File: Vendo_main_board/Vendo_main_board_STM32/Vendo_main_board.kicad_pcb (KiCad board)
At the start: 2 copper layers, 81.1 x 100 mm, 129 parts, among them J1 Screw_Terminal_01x04, J10 Screw_Terminal_01x03, J11 Screw_Terminal_01x02, J12 Screw_Terminal_01x03, J2 Barrel_Jack_MountingPin, J3 Conn_01x05_Pin, J4 Conn_01x05_Pin, J5 BOOT, J6 Screw_Terminal_01x04, J7 FTDI, J9 Conn_01x04_Pin, Q1 Q_NMOS_Depletion_GSD, Q2 Q_NMOS_Depletion_GSD, Q3 Q_NMOS_Depletion_GSD, Q4 Q_NMOS_Depletion_GSD, SW1 SW_Push, SW2 SW_Push, SW3 SW_Push, SW4 SW_Push, SW5 SW_Slide_DPDT, U1 AMS1117-3.3, U2 TPS54331D, U3 STM32F103C8T6, U4 PC817, Y1 32.768kHz, Y2 8MHz

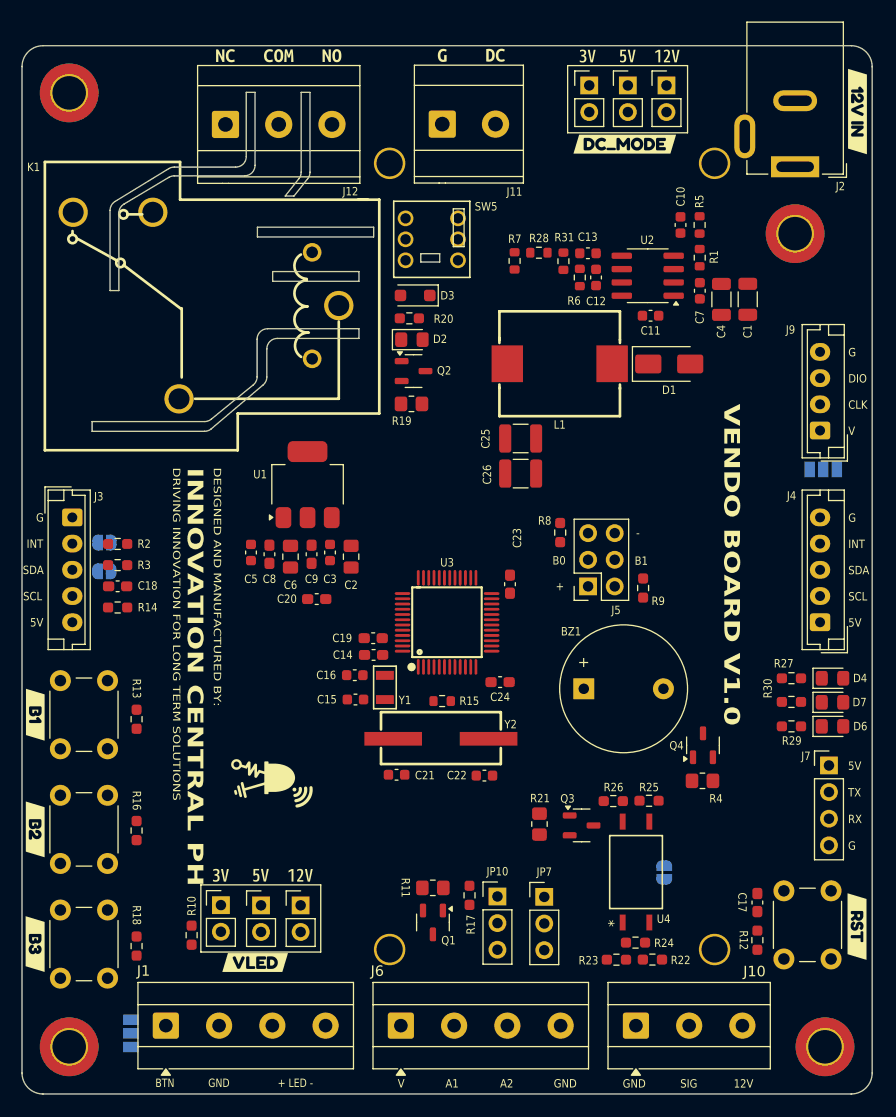
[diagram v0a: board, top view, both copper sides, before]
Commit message: -update pcb placement
- center LCD on pcb
- lcd mounting hole is m3 and 6mm diametr for screw head
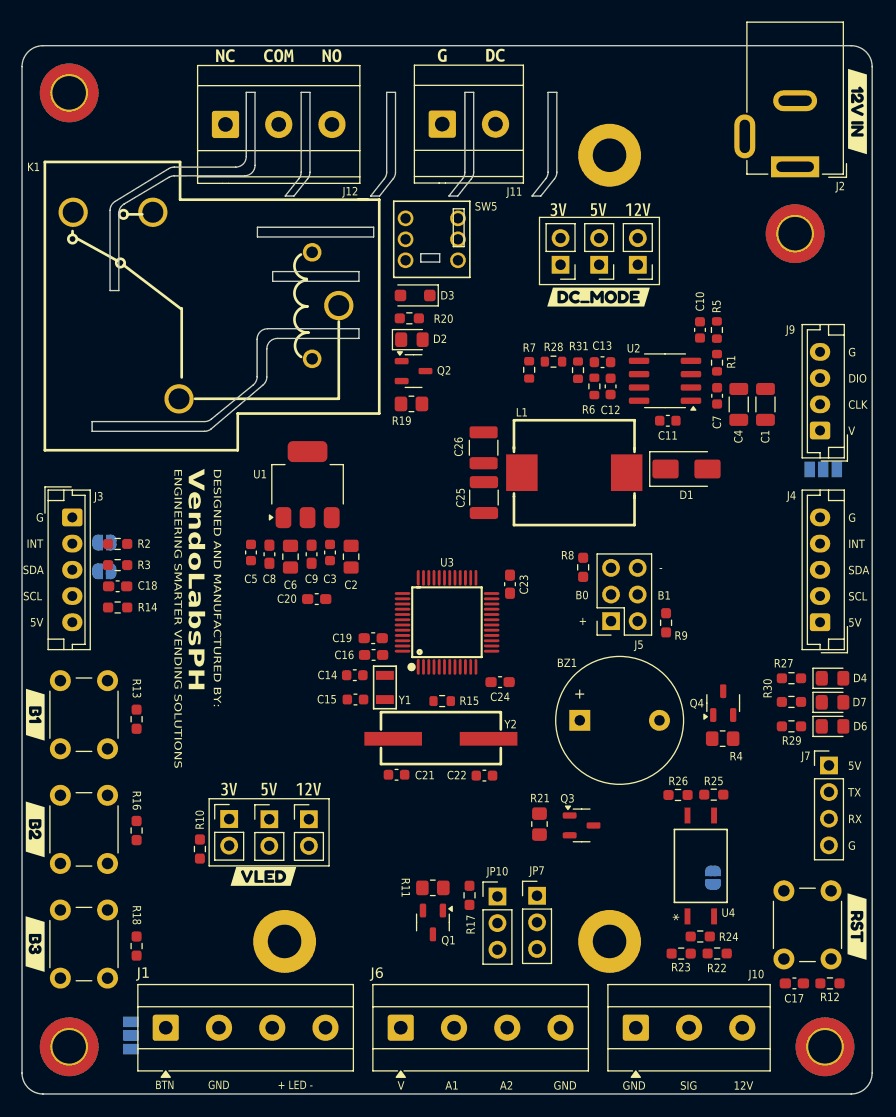
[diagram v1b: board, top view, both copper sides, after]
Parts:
- removed G***: LOGO, InnovKits:innov_logo_5
- moved JP11 19.9 mm to (249.5, 48.5), turned to 180 degrees
- moved JP13 17.7 mm to (256.8, 48.5), turned to 180 degrees
- moved JP12 17.3 mm to (253.2, 48.5), turned to 180 degrees
- moved kibuzzard-6A0C5E83 14.9 mm to (256.9, 43.2)
- moved kibuzzard-6A0C5E92 14.9 mm to (249.3, 43.2)
- moved kibuzzard-6A0C5E89 14.9 mm to (253.1, 43.2)
- moved kibuzzard-6A561C38 14.8 mm to (253.1, 51.6)
- moved L1 10.5 mm to (250.8, 68.3)
- moved R28 10.5 mm to (248.8, 57.7)
- moved C12 10.5 mm to (254.2, 60.1)
- moved C13 10.5 mm to (253.5, 57.8)
- moved R31 10.5 mm to (251.1, 58.5)
- moved R6 10.5 mm to (252.7, 60.1)
- moved R7 10.5 mm to (246.5, 58.5)
- moved C10 10.2 mm to (262.8, 54.7)
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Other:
- outline, holes or cut-outs redrawn
- board text added: "ENGINEERING SMARTER VENDING SOLUTIONS"
- board text added: "VendoLabsPH"
- board text removed: "DRIVING INNOVATION FOR LONG TERM SOLUTIONS"
- board text removed: "INNOVATION CENTRAL PH"

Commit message: - update pcb
- updated pcb placement
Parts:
- J1, J6: footprint TerminalBlock_MetzConnect:TerminalBlock_MetzConnect_Type101_RT01604HBWC_1x04_P5.08mm_Horizontal -> TerminalBlock:TerminalBlock_Xinya_XY308-2.54-4P_1x04_P2.54mm_Horizontal
- J10: footprint TerminalBlock_MetzConnect:TerminalBlock_MetzConnect_Type101_RT01603HBWC_1x03_P5.08mm_Horizontal -> TerminalBlock:TerminalBlock_Xinya_XY308-2.54-3P_1x03_P2.54mm_Horizontal
- moved R25 38.7 mm to (225.6, 102.9), turned to -90 degrees
- moved R26 35.8 mm to (225.6, 106.3), turned to 90 degrees
- moved R5 35.2 mm to (230.9, 65.5), turned to 180 degrees
- moved C10 34.2 mm to (230.9, 67.1), turned to 180 degrees
- moved R4 32.6 mm to (232.5, 97.7), turned to -90 degrees
- moved R1 31.3 mm to (234.0, 65.5), turned to 180 degrees
- moved C1 31.0 mm to (238.0, 60.9), turned to 0 degrees
- moved JP8 30.8 mm to (233.5, 103.0), turned to 180 degrees
- moved U4 30.5 mm to (232.3, 104.2), turned to 180 degrees
- moved Q4 30.0 mm to (235.9, 97.8), turned to 0 degrees
- moved C4 28.5 mm to (238.0, 63.4), turned to 0 degrees
- moved R28 27.7 mm to (233.9, 81.1), turned to 90 degrees
- moved C7 27.6 mm to (237.2, 65.5), turned to 0 degrees
- moved R7 27.5 mm to (234.7, 83.4), turned to 180 degrees
- moved C13 27.0 mm to (234.0, 76.4), turned to -90 degrees
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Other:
- board size 81.1 x 100 mm -> 60 x 100 mm
- board text added: "< BTN >"
- board text removed: "BTN"
- board text removed: "GND"

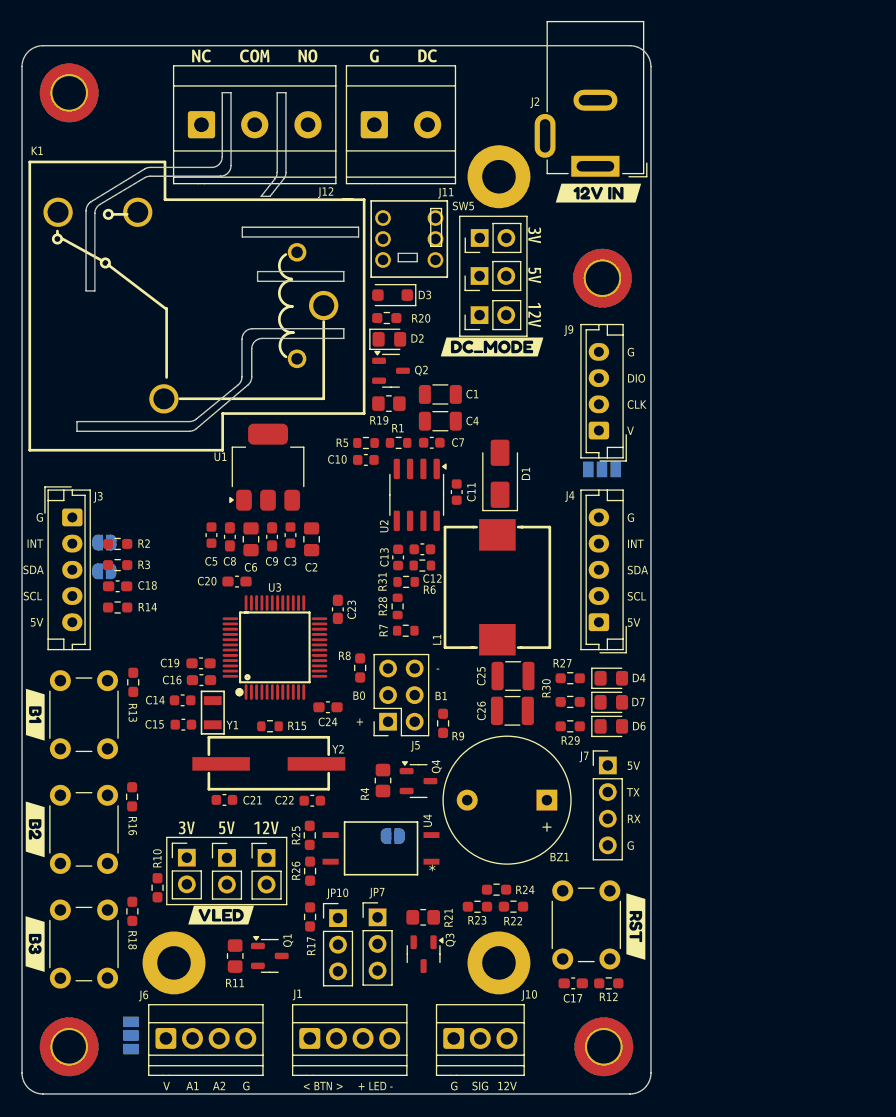
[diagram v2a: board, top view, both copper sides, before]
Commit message: -
-update button mode for relay
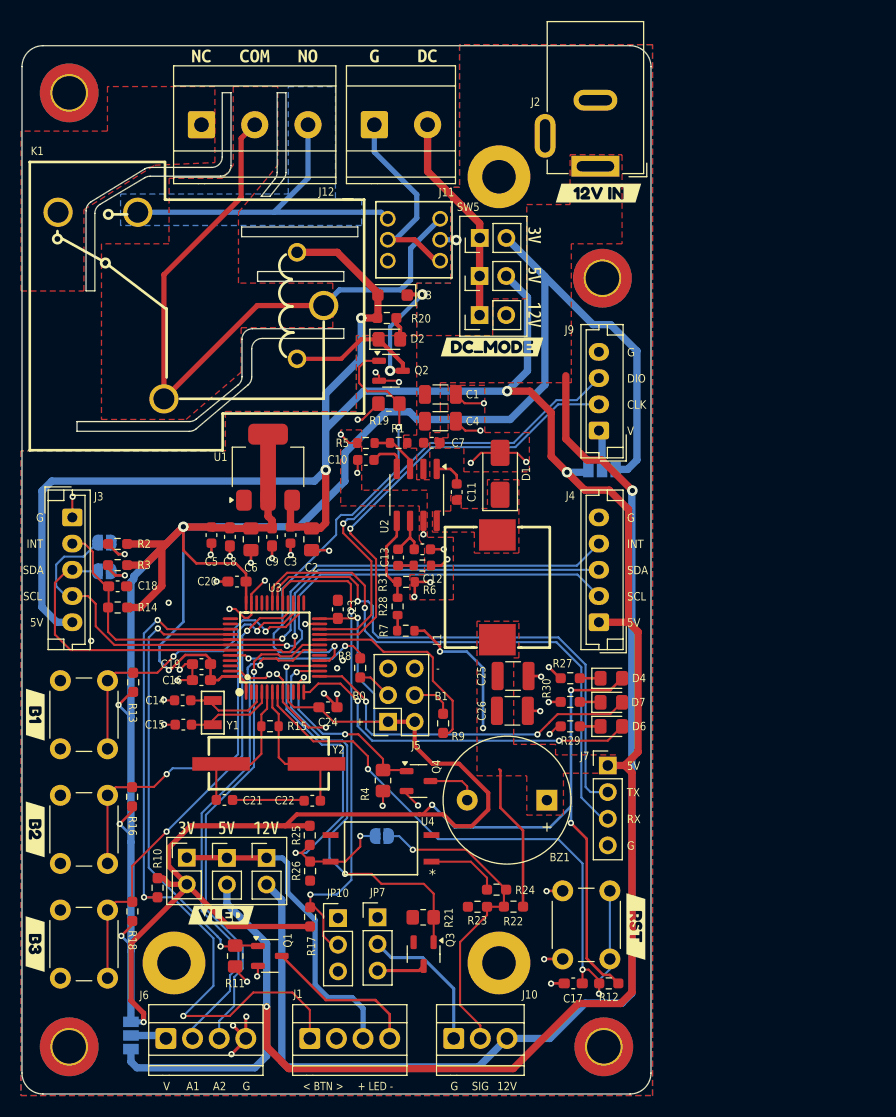
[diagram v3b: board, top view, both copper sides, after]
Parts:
- moved JP8 1.04 mm to (232.4, 103.0)
- moved SW5 0.46 mm to (233.0, 48.1)
- moved C19 0.08 mm to (215.2, 86.6)
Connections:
- SW5 pad 1: RLY_NO -> unconnected-(SW5-A-Pad1)
- SW5 pad 3: unconnected-(SW5-C-Pad3) -> RLY_NO
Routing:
- net +3.3V: track 0.00 -> 385.2 mm, vias 0 -> 10
- net +5V: track 0.00 -> 290.4 mm, vias 0 -> 7
- net +12V: track 0.00 -> 116.4 mm, vias 0 -> 1
- net GND: track 0.00 -> 93.1 mm, vias 0 -> 54
- net USER_BTN: track 0.00 -> 68.9 mm, vias 0 -> 3
- net STM_SCL: track 0.00 -> 68.7 mm, vias 0 -> 1
- net STM_SDA: track 0.00 -> 68.4 mm, vias 0 -> 1
- net RLY_COM: track 0.00 -> 65.0 mm
- net I2C_INT: track 0.00 -> 63.8 mm, vias 0 -> 1
- net STM_RST: track 0.00 -> 62.3 mm, vias 0 -> 3
- net STM_RX: track 0.00 -> 53.6 mm, vias 0 -> 1
- net STM_TX: track 0.00 -> 51.0 mm, vias 0 -> 1
- net AUX_1: track 0.00 -> 48.6 mm, vias 0 -> 1
- net AUX_2: track 0.00 -> 47.5 mm, vias 0 -> 1
- net I2C_CONFG: track 0.00 -> 47.5 mm, vias 0 -> 2
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- added copper zone on F.Cu, net +12V
- added copper zone on F.Cu, net +5V
- added copper zone on F.Cu, net /SW
- added copper zone on B.Cu, net GND
- added copper zone on F.Cu, net GND
- added copper zone on F.Cu, net RLY_COM
- added copper zone on F.Cu, net RLY_NC
- added copper zone on B.Cu, net RLY_NO
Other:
- outline, holes or cut-outs redrawn

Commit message: -done routing vendo stm32 version
- done routing stm32 version
- stm32 version only warning ,clipped silkscreens
- need to note where to put logo, version control and others
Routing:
- net GND: track 93.1 -> 95.3 mm, vias 54 -> 138
- net RLY_DRV: track 45.9 -> 45.3 mm

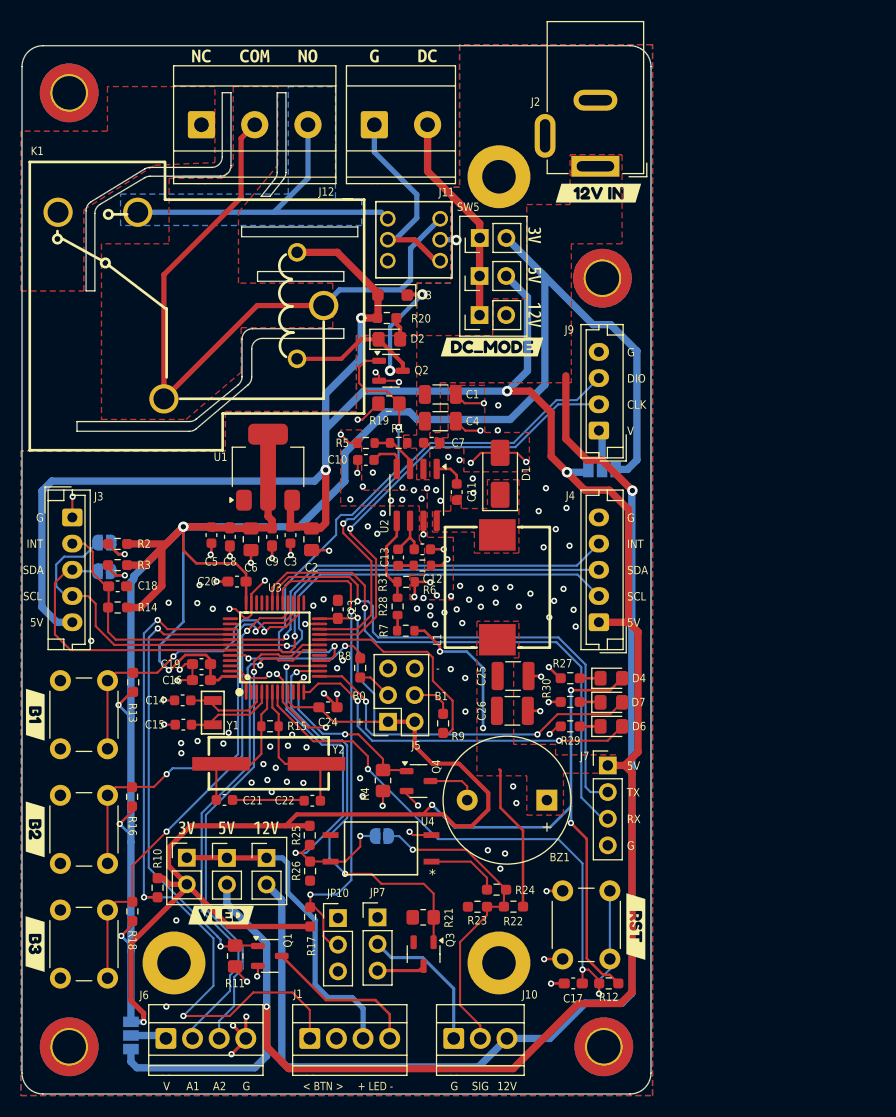
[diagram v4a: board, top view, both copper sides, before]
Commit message: stm32 and esp32 version edit
stm32 ver solid gnd plane to buck conv, adjust buttons to smd , btn1 to 3 and reset
esp32 version adjust slave conn by 1mm far away on the sma hole, adjust button 1 ,2 and reset.
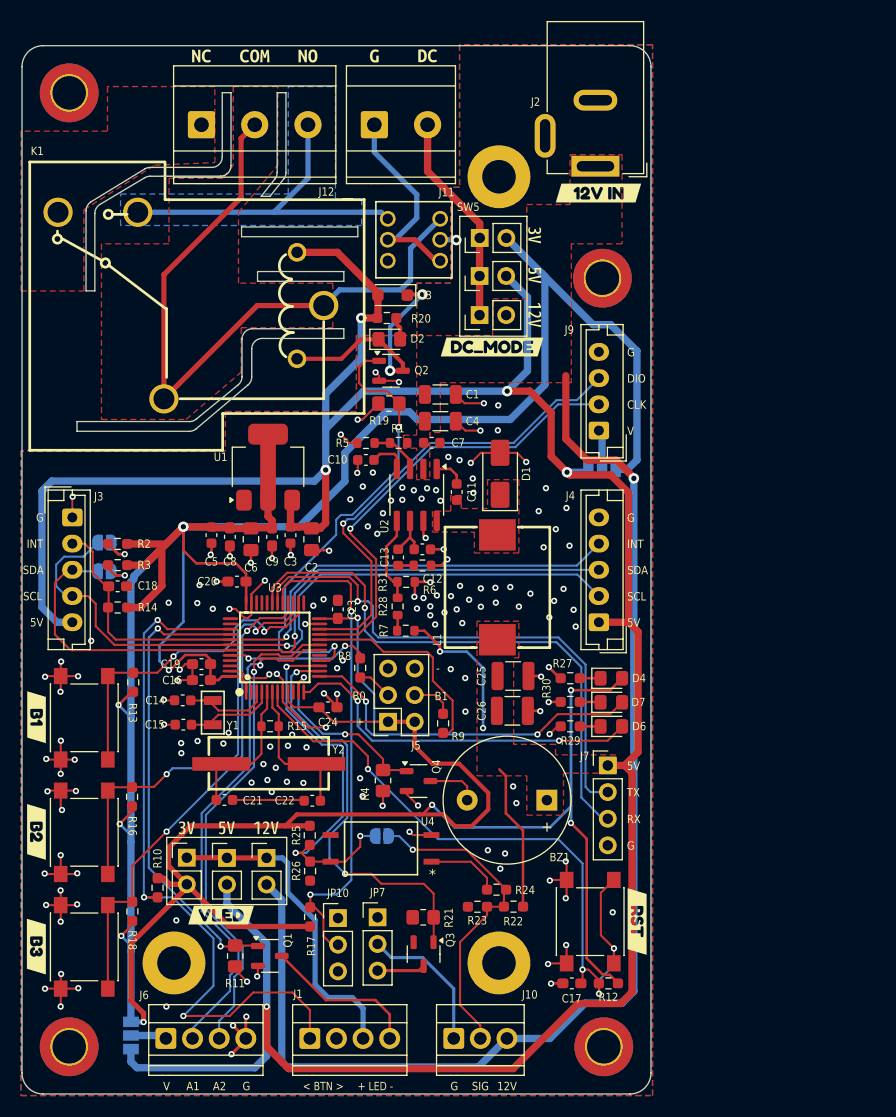
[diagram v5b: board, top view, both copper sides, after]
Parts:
- SW1, SW2, SW3, SW4: footprint Button_Switch_THT:SW_PUSH_6mm_H5mm -> Button_Switch_SMD:SW_SPST_PTS645
- moved SW4 3.75 mm to (204.0, 113.6)
- moved SW3 3.75 mm to (204.0, 102.6)
- moved SW2 3.73 mm to (204.0, 91.7)
- moved SW1 3.49 mm to (252.3, 111.2)
- moved kibuzzard-6A0C536D 0.50 mm to (256.8, 111.2)
- moved kibuzzard-6A0C57AC 0.27 mm to (199.5, 113.5)
- moved kibuzzard-6A0C57A3 0.27 mm to (199.5, 91.7)
- moved kibuzzard-6A0C57A8 0.27 mm to (199.5, 102.6)
- moved C17 0.13 mm to (250.6, 117.0)
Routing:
- net GND: track 95.3 -> 134.9 mm, vias 138 -> 164
- net STM_RST: track 62.3 -> 66.1 mm, vias 3 -> 4
- net BTN_MODE_1: track 30.2 -> 31.4 mm
- net BTN_MODE_2: track 40.1 -> 41.3 mm
- net BTN_MODE_3: track 45.1 -> 46.4 mm
- net +5V: track 290.4 -> 291.3 mm
- net +12V: track 116.4 -> 117.3 mm
